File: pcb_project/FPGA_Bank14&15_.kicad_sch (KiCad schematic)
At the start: 31 parts, among them IC3 IS61WV204816BLL-10TLI, U1 XC7A100T-FTG256, U9 MT25QL128ABA1ESE-0SIT

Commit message: Add most footprints, missing some inductors and 3 buttons
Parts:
- C82: footprint (none) -> Capacitor_SMD:C_1206_3216Metric_Pad1.33x1.80mm_HandSolder
- C83, C84: footprint (none) -> Capacitor_SMD:C_0805_2012Metric_Pad1.18x1.45mm_HandSolder
- C85, C87: footprint (none) -> Capacitor_SMD:C_0603_1608Metric_Pad1.08x0.95mm_HandSolder
- R76, R77, R78, R79, R80, R81, R82, R83, R84: footprint (none) -> Resistor_SMD:R_0805_2012Metric_Pad1.20x1.40mm_HandSolder
- U1: footprint (none) -> Package_BGA:Xilinx_FTG256
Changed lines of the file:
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@@
 			)
 		)
-		(property "Footprint" ""
+		(property "Footprint" "Capacitor_SMD:C_0603_1608Metric_Pad1.08x0.95mm_HandSolder"
 			(at 80.9752 80.01 0)
 			(effects
@@
 			)
 		)
-		(property "Footprint" ""
+		(property "Footprint" "Capacitor_SMD:C_0805_2012Metric_Pad1.18x1.45mm_HandSolder"
 			(at 50.4952 179.07 0)
 			(effects
@@
 			)
 		)
-		(property "Footprint" ""
+		(property "Footprint" "Resistor_SMD:R_0805_2012Metric_Pad1.20x1.40mm_HandSolder"
 			(at 220.472 21.59 90)
 			(effects
@@
 			)
 		)
-		(property "Footprint" ""
+		(property "Footprint" "Resistor_SMD:R_0805_2012Metric_Pad1.20x1.40mm_HandSolder"
 			(at 235.712 21.59 90)
 			(effects
@@
 			)
 		)
-		(property "Footprint" ""
+		(property "Footprint" "Capacitor_SMD:C_0805_2012Metric_Pad1.18x1.45mm_HandSolder"
 			(at 56.8452 179.07 0)
 			(effects
@@
 			)
 		)
-		(property "Footprint" ""
+		(property "Footprint" "Resistor_SMD:R_0805_2012Metric_Pad1.20x1.40mm_HandSolder"
 			(at 215.392 21.59 90)
 			(effects
@@
 			)
 		)
-		(property "Footprint" ""
+		(property "Footprint" "Capacitor_SMD:C_1206_3216Metric_Pad1.33x1.80mm_HandSolder"
 			(at 44.1452 179.07 0)
 			(effects
@@
 			)
 		)
-		(property "Footprint" ""
+		(property "Footprint" "Resistor_SMD:R_0805_2012Metric_Pad1.20x1.40mm_HandSolder"
 			(at 68.072 76.2 90)
 			(effects
@@
 			)
 		)
-		(property "Footprint" ""
+		(property "Footprint" "Resistor_SMD:R_0805_2012Metric_Pad1.20x1.40mm_HandSolder"
 			(at 230.632 21.59 90)
 			(effects
@@
 			)
 		)
-		(property "Footprint" ""
+		(property "Footprint" "Capacitor_SMD:C_0603_1608Metric_Pad1.08x0.95mm_HandSolder"
 			(at 61.9252 179.07 0)
 			(effects
@@
 			)
 		)
-		(property "Footprint" ""
+		(property "Footprint" "Resistor_SMD:R_0805_2012Metric_Pad1.20x1.40mm_HandSolder"
 			(at 89.662 74.93 90)
 			(effects
@@
 			)
 		)
-		(property "Footprint" ""
+		(property "Footprint" "Package_BGA:Xilinx_FTG256"
 			(at 149.86 88.9 0)
 			(effects
@@
 			)
 		)
-		(property "Footprint" ""
+		(property "Footprint" "Resistor_SMD:R_0805_2012Metric_Pad1.20x1.40mm_HandSolder"
 			(at 83.312 74.93 90)
 			(effects
@@
 			)
 		)
-		(property "Footprint" ""
+		(property "Footprint" "Resistor_SMD:R_0805_2012Metric_Pad1.20x1.40mm_HandSolder"
 			(at 225.552 21.59 90)
 			(effects
@@
 			)
 		)
-		(property "Footprint" ""
+		(property "Footprint" "Resistor_SMD:R_0805_2012Metric_Pad1.20x1.40mm_HandSolder"
 			(at 105.41 168.148 90)
 			(effects

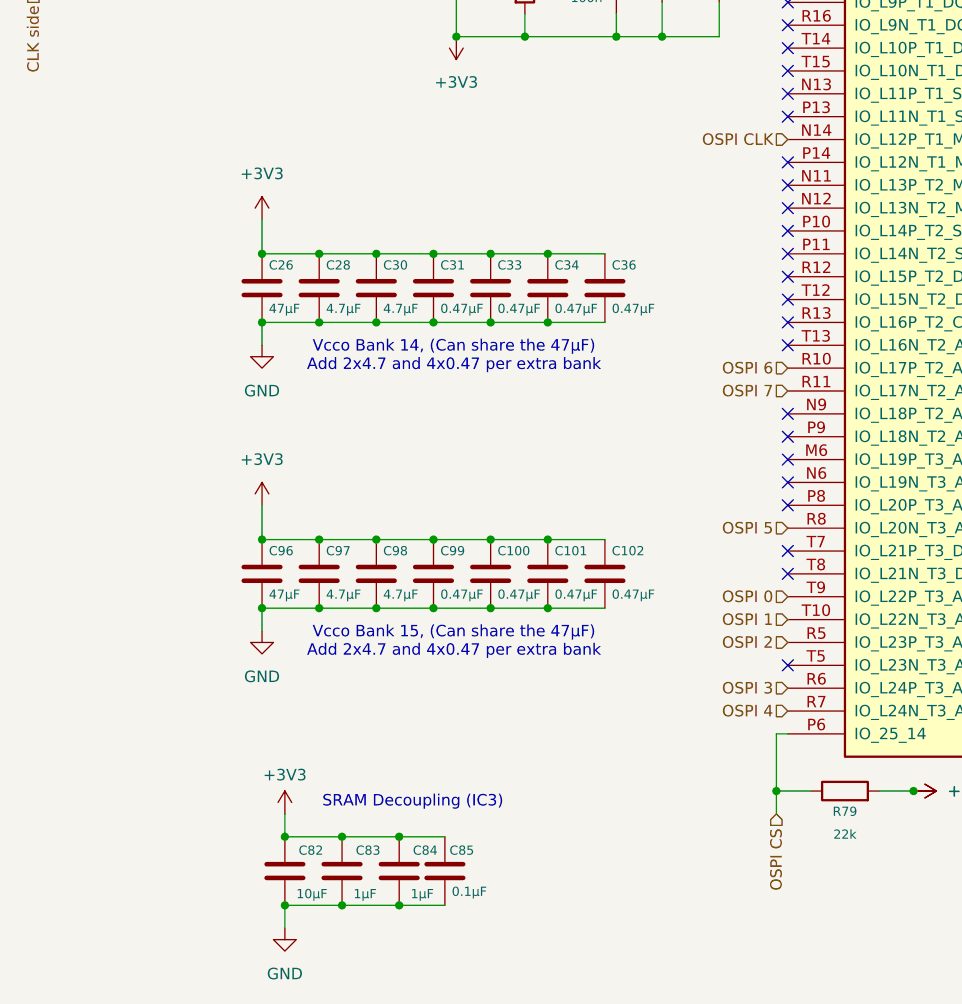
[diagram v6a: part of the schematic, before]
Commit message: Add debounce cap on FPGA reset, add second sram symbol
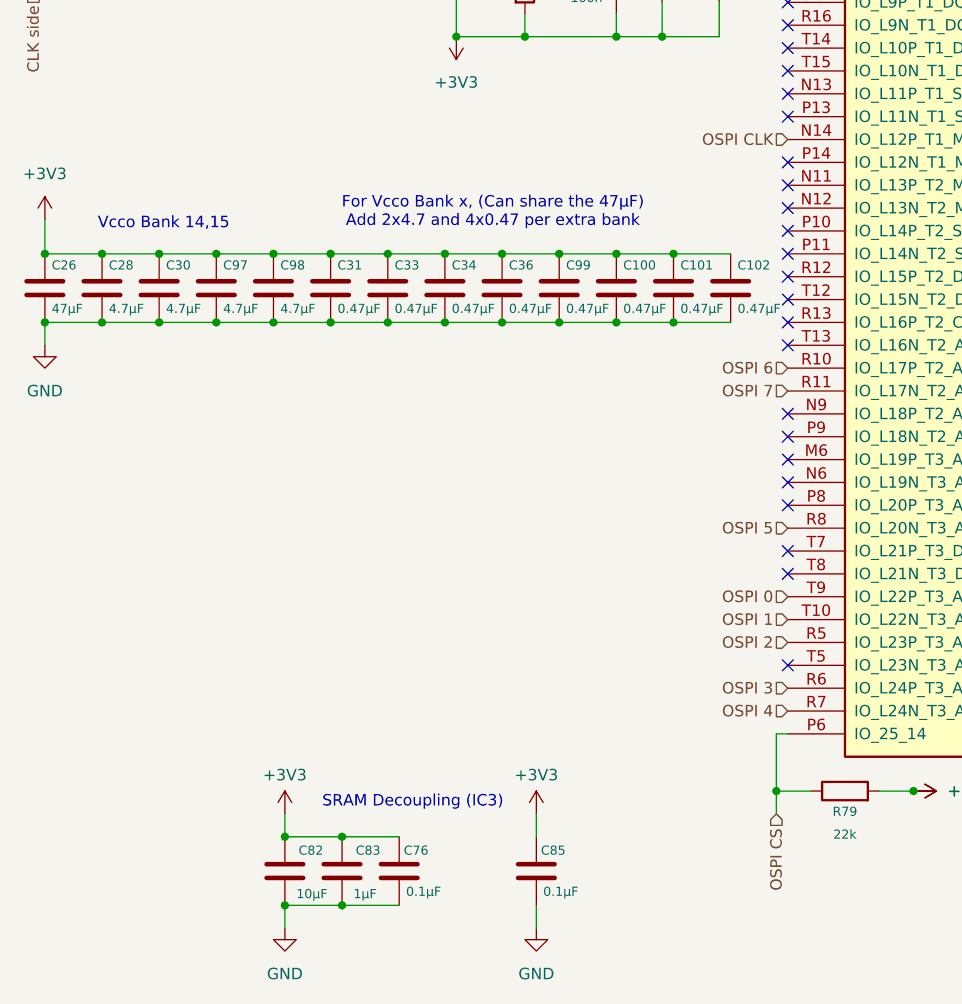
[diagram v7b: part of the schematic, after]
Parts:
- removed C84: 1µF, Capacitor_SMD:C_0805_2012Metric_Pad1.18x1.45mm_HandSolder, symbol Device:C
- removed C96: 47µF, Capacitor_SMD:C_1210_3225Metric_Pad1.33x2.70mm_HandSolder, symbol Device:C
- added C76: 0.1µF, Capacitor_SMD:C_0603_1608Metric_Pad1.08x0.95mm_HandSolder, symbol Device:C
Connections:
- net +3V3: now also C76.1
- net GND: now also C76.2
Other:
- note added: "For Vcco Bank x, (Can share the 47µF) Add 2x4.7 and 4x0.47 per extra bank"
- note added: "Vcco Bank 14,15"
- note removed: "Vcco Bank 14, (Can share the 47µF) Add 2x4.7 and 4x0.47 per extra bank"
- note removed: "Vcco Bank 15, (Can share the 47µF) Add 2x4.7 and 4x0.47 per extra bank"
- moved on the sheet: C100, C101, C102, C26, C28, C30, C31, C33, C34, C36, C85, C97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

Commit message: FPGA decoupler
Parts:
- removed C76: 0.1µF, Capacitor_SMD:C_0603_1608Metric_Pad1.08x0.95mm_HandSolder, symbol Device:C
- added C79 (2-3mm from SRAM Vdd): 0.1µF, Capacitor_SMD:C_0603_1608Metric_Pad1.08x0.95mm_HandSolder, symbol Device:C
- added U5: IS61WV51216BLL-10TLI, TSOP-2_44L_400MIL_ISI, symbol Is61Wv51216BLL:IS61WV51216BLL-10TLI
- C85 (2-3mm from vdd): renamed from C85
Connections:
- net +3V3: now also C79 (2-3mm from SRAM Vdd).1
- net GND: now also C79 (2-3mm from SRAM Vdd).2
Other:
- moved on the sheet: C100, C101, C102, C26, C28, C30, C31, C33, C34, C36, C82, C83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
